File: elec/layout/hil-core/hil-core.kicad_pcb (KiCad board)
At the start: 4 copper layers, 113 parts, among them U4 10µH ±20%

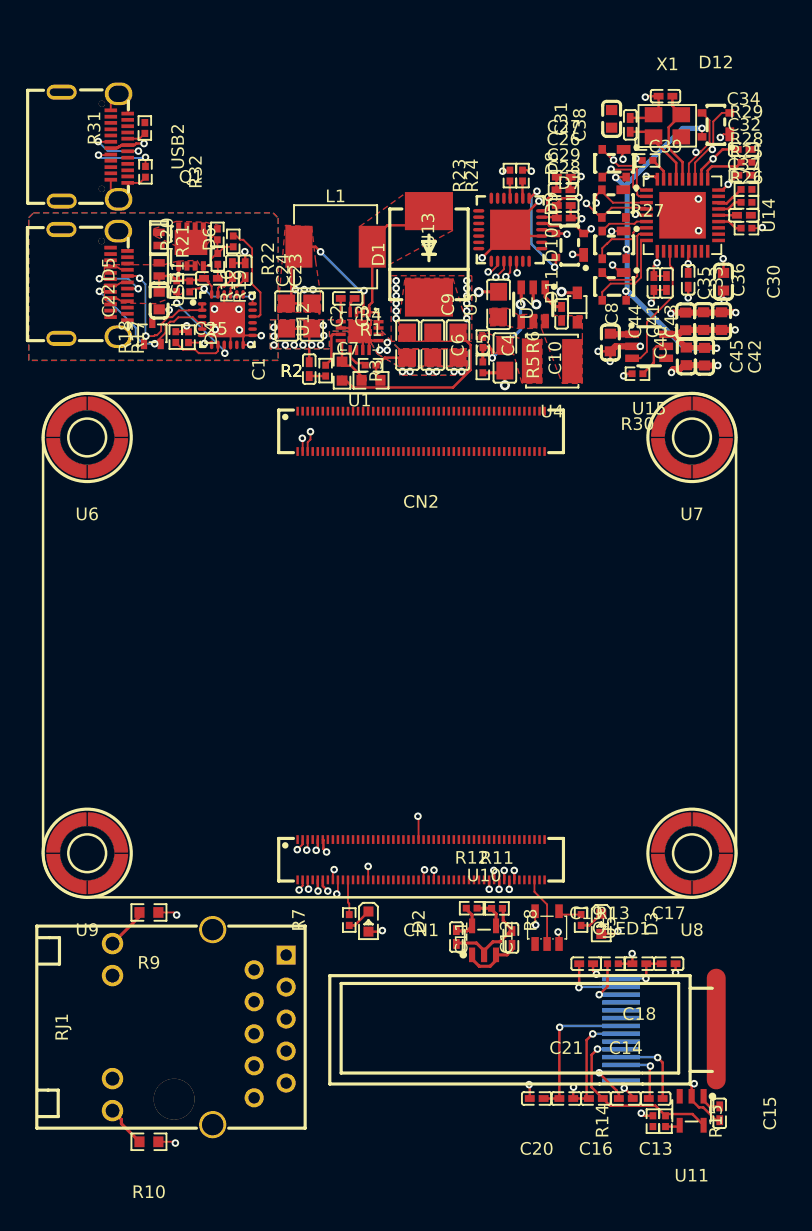
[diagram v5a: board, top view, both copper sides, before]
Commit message: fix shorts in HIL core
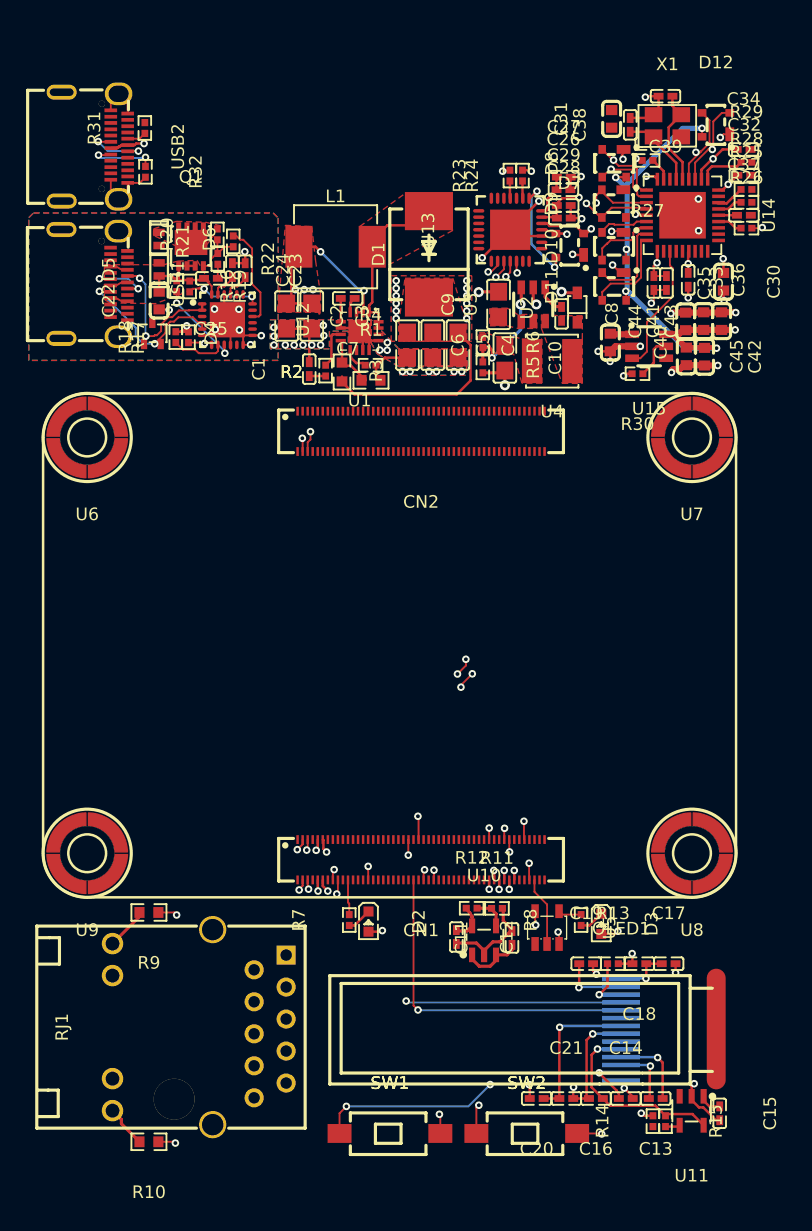
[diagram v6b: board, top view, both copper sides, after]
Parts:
- added SW1: , atopile:SW-SMD_L6.0-W3.3-LS8.0-cfbaed, F.Cu at (149.5, 136.2)
- added SW2: , atopile:SW-SMD_L6.0-W3.3-LS8.0-cfbaed, F.Cu at (160.3, 136.2)
- R13: value 510kΩ ±1% 62.5mW -> 560kΩ ±1% 62.5mW
- R14: value 3.9kΩ ±1% 62.5mW -> 10kΩ ±1% 62.5mW
- R15: value 10kΩ ±1% 62.5mW -> 24.9kΩ ±1% 62.5mW
- moved D10 0.11 mm to (167.2, 65.8)
- moved R2 0.07 mm to (145.7, 75.8)
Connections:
- net A2 renamed usbpd.usb_connector-A2
- net A3 renamed usbpd.usb_connector-A3
- net A8 renamed usbpd.usb_connector-A8
- net B10 renamed usbpd.usb_connector-B10
- net B11 renamed usbpd.usb_connector-B11
- net SBU1 renamed usb_connector.connector-A8
- net SSRXN1 renamed usb_connector.connector-B10
- net SSRXP1 renamed usb_connector.connector-B11
- net SSTXN1 renamed usb_connector.connector-A3
- net SSTXP1 renamed usb_connector.connector-A2
- net SW renamed buck_5v-cathode
- net controller.cm5-line-1 renamed pins[24]
- net controller.cm5-line-2 renamed Y
- net controller.cm5-line-3 renamed controller.cm5-pins[23]
- net controller.cm5-line-4 renamed pins[25]
- net controller.cm5-line-5 renamed controller.cm5-pins[53]
- net controller.cm5-pins[87] renamed controller.cm5-pins[89]
- net controller.cm5-pins[87]-1 renamed pins[87]
- net controller.cm5.hdi_b-pins[40] renamed pins[40]
- net controller.cm5.hdi_b-pins[92] renamed pins[92]
- net pins[23] renamed controller.cm5.hdi_b-pins[23]
- net pins[47] renamed controller.cm5-pins[47]
- net pins[53] renamed controller.cm5-pins[53]-1
- net pins[89] renamed controller.cm5-pins[89]-1
- C10 pad 1: hv-8 -> hv-7
- C11 pad 1: hv-8 -> hv-7
- C12 pad 1: hv -> hv-5
- C15 pad 1: hv-8 -> hv-7
- C16 pad 1: hv-1 -> hv
- C17 pad 1: hv-4 -> hv-3
- C18 pad 1: hv-4 -> hv-3
- C2 pad 1: hv-2 -> hv-4
- C20 pad 1: hv -> hv-5
- C21 pad 1: hv -> hv-5
- C23 pad 2: usbpd.pd_controller-hv -> usbpd.pd_controller-hv-1
- C24 pad 2: usbpd.pd_controller-hv-1 -> usbpd.pd_controller-hv
- C26 pad 1: hv-6 -> hv-9
- C27 pad 1: hv-6 -> hv-9
- C28 pad 1: hv-7 -> hv-6
- C29 pad 1: hv-7 -> hv-6
- C3 pad 1: hv-2 -> hv-4
- C30 pad 1: hv -> hv-5
- C31 pad 1: hv -> hv-5
- C32 pad 1: hv -> hv-5
- C33 pad 1: hv -> hv-5
- C34 pad 1: hv -> hv-5
- C35 pad 1: hv -> hv-5
- C36 pad 1: hv -> hv-5
- C37 pad 1: hv -> hv-5
- C4 pad 1: hv-9 -> hv-8
- C40 pad 1: hv-8 -> hv-7
- C41 pad 1: hv-3 -> hv-2
- C42 pad 1: hv-3 -> hv-2
- C43 pad 1: hv-3 -> hv-2
- C44 pad 1: hv-3 -> hv-2
- C45 pad 1: hv-3 -> hv-2
- C5 pad 1: hv-9 -> hv-8
- C6 pad 1: hv-9 -> hv-8
- C9 pad 1: hv-9 -> hv-8
- CN1 pad 14: controller-line-8 -> controller-line-32
- CN1 pad 15: controller-line-27 -> controller-line-13
- CN1 pad 18: controller-line-18 -> controller-line-8
- CN1 pad 19: controller-line-13 -> controller-line-11
- CN1 pad 2: controller-line-3 -> controller-line-18
- CN1 pad 20: controller-line-7 -> controller-line-16
- CN1 pad 22: controller-line-17 -> controller-line-4
- CN1 pad 23: line-11 -> line-5
- CN1 pad 24: controller.cm5-line -> controller.cm5-pins[47]-1
- CN1 pad 25: line-6 -> line-11
- CN1 pad 28: controller-line-6 -> controller-line-12
- CN1 pad 29: controller-line-2 -> controller-line-9
- CN1 pad 3: controller-line-30 -> controller-line-29
- CN1 pad 39: hv-5 -> hv-1
- CN1 pad 42: hv-5 -> hv-1
- CN1 pad 43: hv-5 -> hv-1
- CN1 pad 46: pins[91] -> controller-line-10
- CN1 pad 5: controller-line-25 -> controller-line-17
- CN1 pad 54: controller.cm5.hdi_a-pins[92] -> controller-line-23
- CN1 pad 57: hv-8 -> hv-7
- CN1 pad 58: hv-8 -> hv-7
- CN1 pad 59: hv-8 -> hv-7
- CN1 pad 6: controller-line-16 -> controller-line-5
- CN1 pad 60: hv-8 -> hv-7
- CN1 pad 61: hv-8 -> hv-7
- CN1 pad 62: hv-8 -> hv-7
- CN1 pad 73: line-4 -> line-6
- CN1 pad 75: line-2 -> line-1
- CN1 pad 77: line-10 -> line-9
- CN1 pad 78: controller.cm5-pins[44] -> controller.cm5-pins[44]-1
- CN1 pad 80: controller.cm5-pins[40] -> controller.cm5-line
- CN1 pad 81: controller-line-23 -> controller-line-28
- CN1 pad 82: controller-line-4 -> controller-line
- CN1 pad 85: controller-line-19 -> controller-line-20
- CN1 pad 87: controller-line-22 -> controller-line-3
- CN1 pad 92: controller-line-1 -> controller-line-31
- CN1 pad 93: controller-line-15 -> controller-line-25
- CN1 pad 95: controller-line -> controller-line-33
- CN1 pad 96: controller-line-24 -> controller-line-27
- CN1 pad 98: controller-line-28 -> controller-line-30
- CN1 pad 99: controller-line-32 -> controller-line-7
- CN2 pad 15: controller-line-10 -> controller-line-34
- CN2 pad 17: controller-line-20 -> controller-line-15
- CN2 pad 18: controller-line-31 -> controller-line-6
- CN2 pad 20: controller-line-12 -> controller-line-35
- CN2 pad 21: controller-line-14 -> controller-line-22
- CN2 pad 65: controller-line-11 -> controller-line-24
- CN2 pad 66: controller-line-5 -> controller-line-1
- CN2 pad 68: controller-line-29 -> controller-line-21
- CN2 pad 69: controller-line-9 -> controller-line-14
- CN2 pad 71: controller-line-21 -> controller-line-19
- CN2 pad 72: controller-line-33 -> controller-line-2
- CN2 pad 78: controller.cm5-pins[44]-1 -> controller.cm5-pins[44]
- CN2 pad 98: line-1 -> line-4
- CN2 pad 99: line-3 -> line-8
- D1 pad 1: hv-9 -> hv-8
- D10 pad 2: usb_hub-line-2 -> usb_hub-line-3
- D10 pad 3: usb_hub-line-4 -> usb_hub-line-2
- D10 pad 4: hv-3 -> hv-2
- D11 pad 2: usb_hub-line -> usb_hub-line-4
- D11 pad 4: hv-3 -> hv-2
- D12 pad 2: line-5 -> line
- D12 pad 3: line-9 -> line-2
- D12 pad 4: hv-3 -> hv-2
- D2 pad 1: controller.cm5-cathode-1 -> controller.cm5-cathode
- D2 pad 2: hv-5 -> hv-1
- D3 pad 1: controller.cm5-cathode -> controller.cm5-cathode-1
- D3 pad 2: hv-5 -> hv-1
- D4 pad 1: usbpd-line-5 -> usbpd-line
- D4 pad 2: usbpd-line-2 -> usbpd-line-5
- D6 pad 1: hv-2 -> hv-4
- D7 pad 2: line-8 -> line-10
- D7 pad 3: line -> line-3
- D7 pad 4: usb_uart-VBUS -> VBUS
- D8 pad 2: line-8 -> line-10
- D8 pad 3: line -> line-3
- D8 pad 4: hv-3 -> hv-2
- D9 pad 2: line-3 -> line-8
- D9 pad 3: line-1 -> line-4
- D9 pad 4: hv-3 -> hv-2
- L1 pad 1: hv-2 -> hv-4
- OLED1 pad 10: line-10 -> line-9
- OLED1 pad 11: line-11 -> line-5
- OLED1 pad 14: hv-4 -> hv-3
- OLED1 pad 5: hv-1 -> hv
- OLED1 pad 8: hv -> hv-5
- Q1 pad 5: hv-2 -> hv-4
- Q1 pad 6: hv-2 -> hv-4
- Q1 pad 7: hv-2 -> hv-4
- Q1 pad 8: hv-2 -> hv-4
- Q1 pad 9: hv-2 -> hv-4
- R10 pad 1: hv-5 -> hv-1
- R10 pad 2: controller.rj45-anode-1 -> controller.rj45-anode
- R12 pad 1: hv -> hv-5
- R15 pad 1: hv-1 -> hv
- R18 pad 1: usbpd-line-4 -> usbpd-line-3
- R2 pad 1: hv-9 -> hv-8
- R20 pad 2: hv-2 -> hv-4
- R24 pad 2: hv-7 -> hv-6
- R25 pad 1: usb_hub.hub-line -> usb_hub.hub-line-1
- R26 pad 1: usb_hub.hub-line-1 -> usb_hub.hub-line
- R6 pad 1: hv-8 -> hv-7
- R7 pad 1: controller.cm5-cathode-1 -> controller.cm5-cathode
- R8 pad 1: controller.cm5-cathode -> controller.cm5-cathode-1
- R9 pad 1: hv-5 -> hv-1
- R9 pad 2: controller.rj45-anode -> controller.rj45-anode-1
- RJ1 pad 11: controller.rj45-anode -> controller.rj45-anode-1
- RJ1 pad 12: controller-line-15 -> controller-line-25
- RJ1 pad 13: controller-line-1 -> controller-line-31
- RJ1 pad 14: controller.rj45-anode-1 -> controller.rj45-anode
- RJ1 pad P1: controller.rj45.connector-net -> controller.rj45.connector-net-1
- RJ1 pad P10: controller.rj45.connector-net-1 -> controller.rj45.connector-net
- RJ1 pad P2: controller-line-16 -> controller-line-5
- RJ1 pad P3: controller-line-25 -> controller-line-17
- RJ1 pad P4: controller-line-3 -> controller-line-18
- RJ1 pad P5: controller-line -> controller-line-33
- RJ1 pad P6: controller-line-24 -> controller-line-27
- RJ1 pad P7: controller-line-30 -> controller-line-29
- RJ1 pad P8: controller-line-32 -> controller-line-7
- RJ1 pad P9: controller-line-28 -> controller-line-30
- U1 pad 2: hv-2 -> hv-4
- U1 pad 3: hv-2 -> hv-4
- U10 pad 1: hv-8 -> hv-7
- U10 pad 3: hv-8 -> hv-7
- U10 pad 5: hv -> hv-5
- U11 pad 1: hv-8 -> hv-7
- U11 pad 3: hv-8 -> hv-7
- U11 pad 5: hv-1 -> hv
- U12 pad 1: usbpd-line-5 -> usbpd-line
- U12 pad 2: usbpd-line-5 -> usbpd-line
- U12 pad 21: usbpd.pd_controller-hv -> usbpd.pd_controller-hv-1
- U12 pad 23: usbpd.pd_controller-hv-1 -> usbpd.pd_controller-hv
- U12 pad 4: usbpd-line-2 -> usbpd-line-5
- U12 pad 5: usbpd-line-2 -> usbpd-line-5
- U12 pad 8: usbpd-line-4 -> usbpd-line-3
- U13 pad 1: usb_uart-line-2 -> usb_uart-line-3
- U13 pad 23: line-6 -> line-11
- U13 pad 25: line-4 -> line-6
- U13 pad 26: line-2 -> line-1
- U13 pad 27: usb_uart-line-3 -> usb_uart-line-1
- U13 pad 28: usb_uart-line-1 -> usb_uart-line-2
- U13 pad 4: line -> line-3
- U13 pad 5: line-8 -> line-10
- U13 pad 6: hv-7 -> hv-6
- U13 pad 7: hv-6 -> hv-9
- U13 pad 8: usb_uart-VBUS -> VBUS
- U14 pad 1: line-8 -> line-10
- U14 pad 10: hv -> hv-5
- U14 pad 12: usb_hub-line-3 -> usb_hub-line
- U14 pad 15: hv -> hv-5
- U14 pad 2: line -> line-3
- U14 pad 22: usb_hub.hub-line-1 -> usb_hub.hub-line
- U14 pad 23: hv -> hv-5
- U14 pad 24: usb_hub.hub-line -> usb_hub.hub-line-1
- U14 pad 27: hv -> hv-5
- U14 pad 29: hv -> hv-5
- U14 pad 3: line-3 -> line-8
- U14 pad 30: line-5 -> line
- U14 pad 31: line-9 -> line-2
- U14 pad 36: hv -> hv-5
- U14 pad 4: line-1 -> line-4
- U14 pad 5: hv -> hv-5
- U14 pad 6: usb_hub-line-2 -> usb_hub-line-3
- U14 pad 7: usb_hub-line-4 -> usb_hub-line-2
- U14 pad 8: usb_hub-line -> usb_hub-line-4
- U15 pad 1: hv-8 -> hv-7
- U15 pad 3: usb_hub-line-3 -> usb_hub-line
- U15 pad 6: hv-3 -> hv-2
- U3 pad 4: hv-9 -> hv-8
- U3 pad 5: hv-9 -> hv-8
- U4 pad 2: hv-8 -> hv-7
- U5 pad 5: hv-5 -> hv-1
- USB1 pad A5: usbpd-line-5 -> usbpd-line
- USB1 pad A6: usbpd-line -> usbpd-line-2
- USB1 pad A7: usbpd-line-3 -> usbpd-line-4
- USB1 pad B5: usbpd-line-2 -> usbpd-line-5
- USB1 pad B6: usbpd-line -> usbpd-line-2
- USB1 pad B7: usbpd-line-3 -> usbpd-line-4
- USB2 pad A4: usb_connector-VBUS -> VBUS
- USB2 pad A6: line-9 -> line-2
- USB2 pad A7: line-5 -> line
- USB2 pad A9: usb_connector-VBUS -> VBUS
- USB2 pad B4: usb_connector-VBUS -> VBUS
- USB2 pad B6: line-9 -> line-2
- USB2 pad B7: line-5 -> line
- USB2 pad B9: usb_connector-VBUS -> VBUS
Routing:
- net (no net): track 207.6 -> 0.00 mm, vias 8 -> 0
- net line-7: track 0.00 -> 55.0 mm, vias 0 -> 2
- net line-2: track 0.00 -> 53.8 mm, vias 0 -> 2
- net line-6: track 0.00 -> 52.1 mm, vias 0 -> 4
- net line-11: track 0.00 -> 49.5 mm, vias 0 -> 4
- net line: track 14.9 -> 58.7 mm, vias 2 -> 3
- net line-4: track 0.00 -> 38.1 mm, vias 0 -> 2
- net hv-3: track 40.8 -> 4.40 mm, vias 6 -> 1
- net controller-line-23: track 0.00 -> 34.7 mm, vias 0 -> 3
- net controller-line-10: track 0.00 -> 29.5 mm, vias 0 -> 2
- net controller-line-31: track 0.00 -> 29.5 mm, vias 0 -> 1
- net controller-line-1: track 29.5 -> 0.00 mm, vias 1 -> 0
- net line-5: track 58.7 -> 30.0 mm, vias 3 -> 2
- net line-9: track 53.8 -> 26.6 mm, vias 2 -> 1
- net controller-line-15: track 24.6 -> 0.00 mm, vias 1 -> 0
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- added copper zone on F.Cu, net hv-4
- added copper zone on F.Cu, net hv-7
- removed copper zone on F.Cu, net hv-2
- removed copper zone on F.Cu, net hv-9

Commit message: Update hil-core layout
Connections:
- net buck_5v-cathode renamed SW
- C10 pad 1: hv-7 -> hv-2
- C11 pad 1: hv-7 -> hv-2
- C12 pad 1: hv-5 -> hv
- C15 pad 1: hv-7 -> hv-2
- C16 pad 1: hv -> hv-7
- C17 pad 1: hv-3 -> hv-4
- C18 pad 1: hv-3 -> hv-4
- C2 pad 1: hv-4 -> hv-1
- C20 pad 1: hv-5 -> hv
- C21 pad 1: hv-5 -> hv
- C26 pad 1: hv-9 -> hv-5
- C27 pad 1: hv-9 -> hv-5
- C28 pad 1: hv-6 -> hv-8
- C29 pad 1: hv-6 -> hv-8
- C3 pad 1: hv-4 -> hv-1
- C30 pad 1: hv-5 -> hv
- C31 pad 1: hv-5 -> hv
- C32 pad 1: hv-5 -> hv
- C33 pad 1: hv-5 -> hv
- C34 pad 1: hv-5 -> hv
- C35 pad 1: hv-5 -> hv
- C36 pad 1: hv-5 -> hv
- C37 pad 1: hv-5 -> hv
- C4 pad 1: hv-8 -> hv-3
- C40 pad 1: hv-7 -> hv-2
- C41 pad 1: hv-2 -> hv-6
- C42 pad 1: hv-2 -> hv-6
- C43 pad 1: hv-2 -> hv-6
- C44 pad 1: hv-2 -> hv-6
- C45 pad 1: hv-2 -> hv-6
- C5 pad 1: hv-8 -> hv-3
- C6 pad 1: hv-8 -> hv-3
- C9 pad 1: hv-8 -> hv-3
- CN1 pad 14: controller-line-32 -> controller-line-15
- CN1 pad 15: controller-line-13 -> controller-line-33
- CN1 pad 19: controller-line-11 -> controller-line-27
- CN1 pad 2: controller-line-18 -> controller-line-29
- CN1 pad 20: controller-line-16 -> controller-line-24
- CN1 pad 22: controller-line-4 -> controller-line-31
- CN1 pad 23: line-5 -> line-7
- CN1 pad 25: line-11 -> line-9
- CN1 pad 27: controller.cm5-pins[53] -> controller.cm5-pins[53]-1
- CN1 pad 28: controller-line-12 -> controller-line-3
- CN1 pad 29: controller-line-9 -> controller-line-12
- CN1 pad 3: controller-line-29 -> controller-line-11
- CN1 pad 39: hv-1 -> hv-9
- CN1 pad 42: hv-1 -> hv-9
- CN1 pad 43: hv-1 -> hv-9
- CN1 pad 44: controller.cm5-pins[89] -> controller.cm5-pins[89]-1
- CN1 pad 45: controller.cm5-pins[89] -> controller.cm5-pins[89]-1
- CN1 pad 46: controller-line-10 -> controller-line-28
- CN1 pad 5: controller-line-17 -> controller-line-9
- CN1 pad 54: controller-line-23 -> controller-line-18
- CN1 pad 57: hv-7 -> hv-2
- CN1 pad 58: hv-7 -> hv-2
- CN1 pad 59: hv-7 -> hv-2
- CN1 pad 6: controller-line-5 -> controller-line-26
- CN1 pad 60: hv-7 -> hv-2
- CN1 pad 61: hv-7 -> hv-2
- CN1 pad 62: hv-7 -> hv-2
- CN1 pad 73: line-6 -> line-1
- CN1 pad 75: line-1 -> line-8
- CN1 pad 77: line-9 -> line-6
- CN1 pad 81: controller-line-28 -> controller-line-34
- CN1 pad 82: controller-line -> controller-line-2
- CN1 pad 83: controller-line-26 -> controller-line-22
- CN1 pad 85: controller-line-20 -> controller-line-1
- CN1 pad 86: line-7 -> line-11
- CN1 pad 87: controller-line-3 -> controller-line-7
- CN1 pad 92: controller-line-31 -> controller-line-6
- CN1 pad 93: controller-line-25 -> controller-line-35
- CN1 pad 95: controller-line-33 -> controller-line-32
- CN1 pad 96: controller-line-27 -> controller-line-13
- CN1 pad 98: controller-line-30 -> controller-line-5
- CN1 pad 99: controller-line-7 -> controller-line-10
- CN2 pad 15: controller-line-34 -> controller-line-21
- CN2 pad 17: controller-line-15 -> controller-line-16
- CN2 pad 18: controller-line-6 -> controller-line-25
- CN2 pad 20: controller-line-35 -> controller-line-23
- CN2 pad 21: controller-line-22 -> controller-line-17
- CN2 pad 27: controller.cm5-pins[53]-1 -> controller.cm5-pins[53]
- CN2 pad 45: controller.cm5-pins[89]-1 -> controller.cm5-pins[89]
- CN2 pad 65: controller-line-24 -> controller-line-30
- CN2 pad 66: controller-line-1 -> controller-line-14
- CN2 pad 68: controller-line-21 -> controller-line-20
- CN2 pad 69: controller-line-14 -> controller-line-19
- CN2 pad 71: controller-line-19 -> controller-line-4
- CN2 pad 72: controller-line-2 -> controller-line
- CN2 pad 98: line-4 -> line-2
- CN2 pad 99: line-8 -> line-4
- D1 pad 1: hv-8 -> hv-3
- D10 pad 2: usb_hub-line-3 -> usb_hub-line-2
- D10 pad 3: usb_hub-line-2 -> usb_hub-line
- D10 pad 4: hv-2 -> hv-6
- D11 pad 2: usb_hub-line-4 -> usb_hub-line-1
- D11 pad 3: usb_hub-line-1 -> usb_hub-line-4
- D11 pad 4: hv-2 -> hv-6
- D12 pad 3: line-2 -> line-5
- D12 pad 4: hv-2 -> hv-6
- D2 pad 1: controller.cm5-cathode -> controller.cm5-cathode-1
- D2 pad 2: hv-1 -> hv-9
- D3 pad 1: controller.cm5-cathode-1 -> controller.cm5-cathode
- D3 pad 2: hv-1 -> hv-9
- D4 pad 1: usbpd-line -> usbpd-line-2
- D4 pad 2: usbpd-line-5 -> usbpd-line-4
- D6 pad 1: hv-4 -> hv-1
- D8 pad 4: hv-2 -> hv-6
- D9 pad 2: line-8 -> line-4
- D9 pad 3: line-4 -> line-2
- D9 pad 4: hv-2 -> hv-6
- L1 pad 1: hv-4 -> hv-1
- OLED1 pad 10: line-9 -> line-6
- OLED1 pad 11: line-5 -> line-7
- OLED1 pad 14: hv-3 -> hv-4
- OLED1 pad 5: hv -> hv-7
- OLED1 pad 8: hv-5 -> hv
- Q1 pad 5: hv-4 -> hv-1
- Q1 pad 6: hv-4 -> hv-1
- Q1 pad 7: hv-4 -> hv-1
- Q1 pad 8: hv-4 -> hv-1
- Q1 pad 9: hv-4 -> hv-1
- R10 pad 1: hv-1 -> hv-9
- R12 pad 1: hv-5 -> hv
- R15 pad 1: hv -> hv-7
- R17 pad 1: usbpd-line-1 -> usbpd-line-5
- R2 pad 1: hv-8 -> hv-3
- R20 pad 2: hv-4 -> hv-1
- R24 pad 2: hv-6 -> hv-8
- R6 pad 1: hv-7 -> hv-2
- R7 pad 1: controller.cm5-cathode -> controller.cm5-cathode-1
- R8 pad 1: controller.cm5-cathode-1 -> controller.cm5-cathode
- R9 pad 1: hv-1 -> hv-9
- RJ1 pad 12: controller-line-25 -> controller-line-35
- RJ1 pad 13: controller-line-31 -> controller-line-6
- RJ1 pad P2: controller-line-5 -> controller-line-26
- RJ1 pad P3: controller-line-17 -> controller-line-9
- RJ1 pad P4: controller-line-18 -> controller-line-29
- RJ1 pad P5: controller-line-33 -> controller-line-32
- RJ1 pad P6: controller-line-27 -> controller-line-13
- RJ1 pad P7: controller-line-29 -> controller-line-11
- RJ1 pad P8: controller-line-7 -> controller-line-10
- RJ1 pad P9: controller-line-30 -> controller-line-5
- SW1 pad 1: controller-line-23 -> controller-line-18
- SW2 pad 1: controller-line-10 -> controller-line-28
- U1 pad 2: hv-4 -> hv-1
- U1 pad 3: hv-4 -> hv-1
- U10 pad 1: hv-7 -> hv-2
- U10 pad 3: hv-7 -> hv-2
- U10 pad 5: hv-5 -> hv
- U11 pad 1: hv-7 -> hv-2
- U11 pad 3: hv-7 -> hv-2
- U11 pad 5: hv -> hv-7
- U12 pad 1: usbpd-line -> usbpd-line-2
- U12 pad 2: usbpd-line -> usbpd-line-2
- U12 pad 4: usbpd-line-5 -> usbpd-line-4
- U12 pad 5: usbpd-line-5 -> usbpd-line-4
- U12 pad 7: usbpd-line-1 -> usbpd-line-5
- U13 pad 1: usb_uart-line-3 -> usb_uart-line-2
- U13 pad 2: usb_uart-line -> usb_uart-line-3
- U13 pad 23: line-11 -> line-9
- U13 pad 24: line-7 -> line-11
- U13 pad 25: line-6 -> line-1
- U13 pad 26: line-1 -> line-8
- U13 pad 27: usb_uart-line-1 -> usb_uart-line
- U13 pad 28: usb_uart-line-2 -> usb_uart-line-1
- U13 pad 6: hv-6 -> hv-8
- U13 pad 7: hv-9 -> hv-5
- U14 pad 10: hv-5 -> hv
- U14 pad 12: usb_hub-line -> usb_hub-line-3
- U14 pad 15: hv-5 -> hv
- U14 pad 23: hv-5 -> hv
- U14 pad 27: hv-5 -> hv
- U14 pad 29: hv-5 -> hv
- U14 pad 3: line-8 -> line-4
- U14 pad 31: line-2 -> line-5
- U14 pad 36: hv-5 -> hv
- U14 pad 4: line-4 -> line-2
- U14 pad 5: hv-5 -> hv
- U14 pad 6: usb_hub-line-3 -> usb_hub-line-2
- U14 pad 7: usb_hub-line-2 -> usb_hub-line
- U14 pad 8: usb_hub-line-4 -> usb_hub-line-1
- U14 pad 9: usb_hub-line-1 -> usb_hub-line-4
- U15 pad 1: hv-7 -> hv-2
- U15 pad 3: usb_hub-line -> usb_hub-line-3
- U15 pad 6: hv-2 -> hv-6
- U3 pad 4: hv-8 -> hv-3
- U3 pad 5: hv-8 -> hv-3
- U4 pad 2: hv-7 -> hv-2
- U5 pad 5: hv-1 -> hv-9
- USB1 pad A5: usbpd-line -> usbpd-line-2
- USB1 pad A6: usbpd-line-2 -> usbpd-line
- USB1 pad A7: usbpd-line-4 -> usbpd-line-1
- USB1 pad B5: usbpd-line-5 -> usbpd-line-4
- USB1 pad B6: usbpd-line-2 -> usbpd-line
- USB1 pad B7: usbpd-line-4 -> usbpd-line-1
- USB2 pad A6: line-2 -> line-5
- USB2 pad B6: line-2 -> line-5
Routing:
- net hv-6: track 6.02 -> 40.8 mm, vias 2 -> 6
- net controller-line-23: track 34.7 -> 0.00 mm, vias 3 -> 0
- net controller-line-28: track 0.00 -> 29.5 mm, vias 0 -> 2
- net controller-line-6: track 0.00 -> 29.5 mm, vias 0 -> 1
- net controller-line-31: track 29.5 -> 0.00 mm, vias 1 -> 0
- net hv-2: track 40.8 -> 13.1 mm
- net hv-5: track 30.5 -> 3.36 mm, vias 8 -> 0
- net line-6: track 52.1 -> 26.6 mm, vias 4 -> 1
- net line-7: track 55.0 -> 30.0 mm
- net controller-line-35: track 0.00 -> 24.6 mm, vias 0 -> 1
- net controller-line-25: track 24.6 -> 0.00 mm, vias 1 -> 0
- net line-5: track 30.0 -> 53.8 mm
- net line-9: track 26.6 -> 49.5 mm, vias 1 -> 4
- net controller-line-9: track 0.00 -> 19.6 mm, vias 0 -> 1
- net controller-line-17: track 19.6 -> 0.00 mm, vias 1 -> 0
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- added copper zone on F.Cu, net hv-1
- added copper zone on F.Cu, net hv-2
- added copper zone on F.Cu, net hv-3
- removed copper zone on F.Cu, net hv-4
- removed copper zone on F.Cu, net hv-7
- removed copper zone on F.Cu, net hv-8

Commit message: update HIL core layout, again
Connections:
- net controller.cm5-pins[89] renamed pins[89]
- net controller.cm5-pins[89]-1 renamed controller.cm5-pins[87]
- net pins[87] renamed controller.cm5-pins[87]-1
- net usb_connector.connector-A10 renamed usb_connector.connector-SSRXN2
- net usb_connector.connector-A11 renamed usb_connector.connector-SSRXP2
- net usb_connector.connector-B2 renamed usb_connector.connector-SSTXP2
- net usb_connector.connector-B3 renamed usb_connector.connector-SSTXN2
- net usb_connector.connector-B8 renamed usb_connector.connector-SBU2
- net usbpd.usb_connector-A10 renamed usbpd.usb_connector-SSRXN2
- net usbpd.usb_connector-A11 renamed usbpd.usb_connector-SSRXP2
- net usbpd.usb_connector-B2 renamed usbpd.usb_connector-SSTXP2
- net usbpd.usb_connector-B3 renamed usbpd.usb_connector-SSTXN2
- net usbpd.usb_connector-B8 renamed usbpd.usb_connector-SBU2
- C10 pad 1: hv-2 -> hv-3
- C11 pad 1: hv-2 -> hv-3
- C12 pad 1: hv -> hv-9
- C15 pad 1: hv-2 -> hv-3
- C16 pad 1: hv-7 -> hv-6
- C17 pad 1: hv-4 -> hv-8
- C18 pad 1: hv-4 -> hv-8
- C2 pad 1: hv-1 -> hv-4
- C20 pad 1: hv -> hv-9
- C21 pad 1: hv -> hv-9
- C23 pad 2: usbpd.pd_controller-hv-1 -> usbpd.pd_controller-hv
- C24 pad 2: usbpd.pd_controller-hv -> usbpd.pd_controller-hv-1
- C26 pad 1: hv-5 -> hv-2
- C27 pad 1: hv-5 -> hv-2
- C28 pad 1: hv-8 -> hv
- C29 pad 1: hv-8 -> hv
- C3 pad 1: hv-1 -> hv-4
- C30 pad 1: hv -> hv-9
- C31 pad 1: hv -> hv-9
- C32 pad 1: hv -> hv-9
- C33 pad 1: hv -> hv-9
- C34 pad 1: hv -> hv-9
- C35 pad 1: hv -> hv-9
- C36 pad 1: hv -> hv-9
- C37 pad 1: hv -> hv-9
- C4 pad 1: hv-3 -> hv-7
- C40 pad 1: hv-2 -> hv-3
- C41 pad 1: hv-6 -> hv-1
- C42 pad 1: hv-6 -> hv-1
- C43 pad 1: hv-6 -> hv-1
- C44 pad 1: hv-6 -> hv-1
- C45 pad 1: hv-6 -> hv-1
- C5 pad 1: hv-3 -> hv-7
- C6 pad 1: hv-3 -> hv-7
- C9 pad 1: hv-3 -> hv-7
- CN1 pad 14: controller-line-15 -> controller-line-33
- CN1 pad 15: controller-line-33 -> controller-line-9
- CN1 pad 18: controller-line-8 -> controller-line-27
- CN1 pad 19: controller-line-27 -> controller-line-15
- CN1 pad 2: controller-line-29 -> controller-line-1
- CN1 pad 20: controller-line-24 -> controller-line-16
- CN1 pad 22: controller-line-31 -> controller-line-6
- CN1 pad 23: line-7 -> line-1
- CN1 pad 25: line-9 -> line-4
- CN1 pad 28: controller-line-3 -> controller-line-35
- CN1 pad 29: controller-line-12 -> controller-line-10
- CN1 pad 3: controller-line-11 -> controller-line-29
- CN1 pad 39: hv-9 -> hv-5
- CN1 pad 42: hv-9 -> hv-5
- CN1 pad 43: hv-9 -> hv-5
- CN1 pad 46: controller-line-28 -> controller-line-7
- CN1 pad 5: controller-line-9 -> controller-line-8
- CN1 pad 54: controller-line-18 -> controller-line-2
- CN1 pad 57: hv-2 -> hv-3
- CN1 pad 58: hv-2 -> hv-3
- CN1 pad 59: hv-2 -> hv-3
- CN1 pad 6: controller-line-26 -> controller-line-22
- CN1 pad 60: hv-2 -> hv-3
- CN1 pad 61: hv-2 -> hv-3
- CN1 pad 62: hv-2 -> hv-3
- CN1 pad 73: line-1 -> line-6
- CN1 pad 75: line-8 -> line-11
- CN1 pad 77: line-6 -> line-10
- CN1 pad 81: controller-line-34 -> controller-line-21
- CN1 pad 82: controller-line-2 -> controller-line-11
- CN1 pad 83: controller-line-22 -> controller-line-18
- CN1 pad 85: controller-line-1 -> controller-line-13
- CN1 pad 86: line-11 -> line-9
- CN1 pad 87: controller-line-7 -> controller-line-32
- CN1 pad 92: controller-line-6 -> controller-line-17
- CN1 pad 93: controller-line-35 -> controller-line-34
- CN1 pad 95: controller-line-32 -> controller-line-25
- CN1 pad 96: controller-line-13 -> controller-line-14
- CN1 pad 98: controller-line-5 -> controller-line
- CN1 pad 99: controller-line-10 -> controller-line-31
- CN2 pad 15: controller-line-21 -> controller-line-4
- CN2 pad 17: controller-line-16 -> controller-line-5
- CN2 pad 18: controller-line-25 -> controller-line-23
- CN2 pad 20: controller-line-23 -> controller-line-20
- CN2 pad 21: controller-line-17 -> controller-line-26
- CN2 pad 65: controller-line-30 -> controller-line-19
- CN2 pad 66: controller-line-14 -> controller-line-3
- CN2 pad 68: controller-line-20 -> controller-line-28
- CN2 pad 69: controller-line-19 -> controller-line-24
- CN2 pad 71: controller-line-4 -> controller-line-30
- CN2 pad 72: controller-line -> controller-line-12
- CN2 pad 98: line-2 -> line-3
- CN2 pad 99: line-4 -> line
- D1 pad 1: hv-3 -> hv-7
- D10 pad 2: usb_hub-line-2 -> usb_hub-line-4
- D10 pad 3: usb_hub-line -> usb_hub-line-3
- D10 pad 4: hv-6 -> hv-1
- D11 pad 3: usb_hub-line-4 -> usb_hub-line-2
- D11 pad 4: hv-6 -> hv-1
- D12 pad 2: line -> line-5
- D12 pad 3: line-5 -> line-2
- D12 pad 4: hv-6 -> hv-1
- D2 pad 1: controller.cm5-cathode-1 -> controller.cm5-cathode
- D2 pad 2: hv-9 -> hv-5
- D3 pad 1: controller.cm5-cathode -> controller.cm5-cathode-1
- D3 pad 2: hv-9 -> hv-5
- D4 pad 1: usbpd-line-2 -> usbpd-line-3
- D4 pad 2: usbpd-line-4 -> usbpd-line-2
- D6 pad 1: hv-1 -> hv-4
- D7 pad 2: line-10 -> line-7
- D7 pad 3: line-3 -> line-8
- D8 pad 2: line-10 -> line-7
- D8 pad 3: line-3 -> line-8
- D8 pad 4: hv-6 -> hv-1
- D9 pad 2: line-4 -> line
- D9 pad 3: line-2 -> line-3
- D9 pad 4: hv-6 -> hv-1
- L1 pad 1: hv-1 -> hv-4
- OLED1 pad 10: line-6 -> line-10
- OLED1 pad 11: line-7 -> line-1
- OLED1 pad 14: hv-4 -> hv-8
- OLED1 pad 5: hv-7 -> hv-6
- OLED1 pad 8: hv -> hv-9
- Q1 pad 5: hv-1 -> hv-4
- Q1 pad 6: hv-1 -> hv-4
- Q1 pad 7: hv-1 -> hv-4
- Q1 pad 8: hv-1 -> hv-4
- Q1 pad 9: hv-1 -> hv-4
- R10 pad 1: hv-9 -> hv-5
- R10 pad 2: controller.rj45-anode -> controller.rj45-anode-1
- R12 pad 1: hv -> hv-9
- R15 pad 1: hv-7 -> hv-6
- R17 pad 1: usbpd-line-5 -> usbpd-line-4
- R18 pad 1: usbpd-line-3 -> usbpd-line
- R2 pad 1: hv-3 -> hv-7
- R20 pad 2: hv-1 -> hv-4
- R24 pad 2: hv-8 -> hv
- R25 pad 1: usb_hub.hub-line-1 -> usb_hub.hub-line
- R26 pad 1: usb_hub.hub-line -> usb_hub.hub-line-1
- R6 pad 1: hv-2 -> hv-3
- R7 pad 1: controller.cm5-cathode-1 -> controller.cm5-cathode
- R8 pad 1: controller.cm5-cathode -> controller.cm5-cathode-1
- R9 pad 1: hv-9 -> hv-5
- R9 pad 2: controller.rj45-anode-1 -> controller.rj45-anode
- RJ1 pad 11: controller.rj45-anode-1 -> controller.rj45-anode
- RJ1 pad 12: controller-line-35 -> controller-line-34
- RJ1 pad 13: controller-line-6 -> controller-line-17
- RJ1 pad 14: controller.rj45-anode -> controller.rj45-anode-1
- RJ1 pad P1: controller.rj45.connector-net-1 -> controller.rj45.connector-net
- RJ1 pad P10: controller.rj45.connector-net -> controller.rj45.connector-net-1
- RJ1 pad P2: controller-line-26 -> controller-line-22
- RJ1 pad P3: controller-line-9 -> controller-line-8
- RJ1 pad P4: controller-line-29 -> controller-line-1
- RJ1 pad P5: controller-line-32 -> controller-line-25
- RJ1 pad P6: controller-line-13 -> controller-line-14
- RJ1 pad P7: controller-line-11 -> controller-line-29
- RJ1 pad P8: controller-line-10 -> controller-line-31
- RJ1 pad P9: controller-line-5 -> controller-line
- SW1 pad 1: controller-line-18 -> controller-line-2
- SW2 pad 1: controller-line-28 -> controller-line-7
- U1 pad 2: hv-1 -> hv-4
- U1 pad 3: hv-1 -> hv-4
- U10 pad 1: hv-2 -> hv-3
- U10 pad 3: hv-2 -> hv-3
- U10 pad 5: hv -> hv-9
- U11 pad 1: hv-2 -> hv-3
- U11 pad 3: hv-2 -> hv-3
- U11 pad 5: hv-7 -> hv-6
- U12 pad 1: usbpd-line-2 -> usbpd-line-3
- U12 pad 2: usbpd-line-2 -> usbpd-line-3
- U12 pad 21: usbpd.pd_controller-hv-1 -> usbpd.pd_controller-hv
- U12 pad 23: usbpd.pd_controller-hv -> usbpd.pd_controller-hv-1
- U12 pad 4: usbpd-line-4 -> usbpd-line-2
- U12 pad 5: usbpd-line-4 -> usbpd-line-2
- U12 pad 7: usbpd-line-5 -> usbpd-line-4
- U12 pad 8: usbpd-line-3 -> usbpd-line
- U13 pad 23: line-9 -> line-4
- U13 pad 24: line-11 -> line-9
- U13 pad 25: line-1 -> line-6
- U13 pad 26: line-8 -> line-11
- U13 pad 27: usb_uart-line -> usb_uart-line-1
- U13 pad 28: usb_uart-line-1 -> usb_uart-line
- U13 pad 4: line-3 -> line-8
- U13 pad 5: line-10 -> line-7
- U13 pad 6: hv-8 -> hv
- U13 pad 7: hv-5 -> hv-2
- U14 pad 1: line-10 -> line-7
- U14 pad 10: hv -> hv-9
- U14 pad 12: usb_hub-line-3 -> usb_hub-line
- U14 pad 15: hv -> hv-9
- U14 pad 2: line-3 -> line-8
- U14 pad 22: usb_hub.hub-line -> usb_hub.hub-line-1
- U14 pad 23: hv -> hv-9
- U14 pad 24: usb_hub.hub-line-1 -> usb_hub.hub-line
- U14 pad 27: hv -> hv-9
- U14 pad 29: hv -> hv-9
- U14 pad 3: line-4 -> line
- U14 pad 30: line -> line-5
- U14 pad 31: line-5 -> line-2
- U14 pad 36: hv -> hv-9
- U14 pad 4: line-2 -> line-3
- U14 pad 5: hv -> hv-9
- U14 pad 6: usb_hub-line-2 -> usb_hub-line-4
- U14 pad 7: usb_hub-line -> usb_hub-line-3
- U14 pad 9: usb_hub-line-4 -> usb_hub-line-2
- U15 pad 1: hv-2 -> hv-3
- U15 pad 3: usb_hub-line-3 -> usb_hub-line
- U15 pad 6: hv-6 -> hv-1
- U3 pad 4: hv-3 -> hv-7
- U3 pad 5: hv-3 -> hv-7
- U4 pad 2: hv-2 -> hv-3
- U5 pad 5: hv-9 -> hv-5
- USB1 pad A5: usbpd-line-2 -> usbpd-line-3
- USB1 pad A6: usbpd-line -> usbpd-line-1
- USB1 pad A7: usbpd-line-1 -> usbpd-line-5
- USB1 pad B5: usbpd-line-4 -> usbpd-line-2
- USB1 pad B6: usbpd-line -> usbpd-line-1
- USB1 pad B7: usbpd-line-1 -> usbpd-line-5
- USB2 pad A6: line-5 -> line-2
- USB2 pad A7: line -> line-5
- USB2 pad B6: line-5 -> line-2
- USB2 pad B7: line -> line-5
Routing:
- net line-8: track 53.4 -> 14.9 mm
- net controller-line-2: track 0.00 -> 34.7 mm, vias 0 -> 3
- net controller-line-18: track 34.7 -> 0.00 mm, vias 3 -> 0
- net controller-line-7: track 0.00 -> 29.5 mm, vias 0 -> 2
- net controller-line-28: track 29.5 -> 0.00 mm, vias 2 -> 0
- net controller-line-6: track 29.5 -> 0.00 mm, vias 1 -> 0
- net controller-line-17: track 0.00 -> 29.5 mm, vias 0 -> 1
- net line-6: track 26.6 -> 52.1 mm, vias 1 -> 4
- net hv-6: track 40.8 -> 15.4 mm, vias 6 -> 1
- net controller-line-35: track 24.6 -> 0.00 mm, vias 1 -> 0
- net controller-line-34: track 0.00 -> 24.6 mm, vias 0 -> 1
- net hv: track 30.5 -> 6.02 mm, vias 8 -> 2
- net hv-1: track 17.0 -> 40.8 mm, vias 5 -> 6
- net line-3: track 14.9 -> 38.1 mm
- net line-1: track 52.1 -> 30.0 mm, vias 4 -> 2
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- added copper zone on F.Cu, net hv-4
- added copper zone on F.Cu, net hv-7
- removed copper zone on F.Cu, net hv-1
- removed copper zone on F.Cu, net hv-2
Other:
- board outline added: 1.5 x 9.6 mm
